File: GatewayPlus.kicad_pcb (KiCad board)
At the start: 2 copper layers, 104.7 x 63.4 mm, 31 parts, among them J1 LTDC_LCD_FPC_40p, SW1 SW_Push, U1 STM32F429IGTx, U2 IS42S16400J - HY57V641620E, U3 W25Q128JVS, Y1 32.768KHz, Y2 25MHz

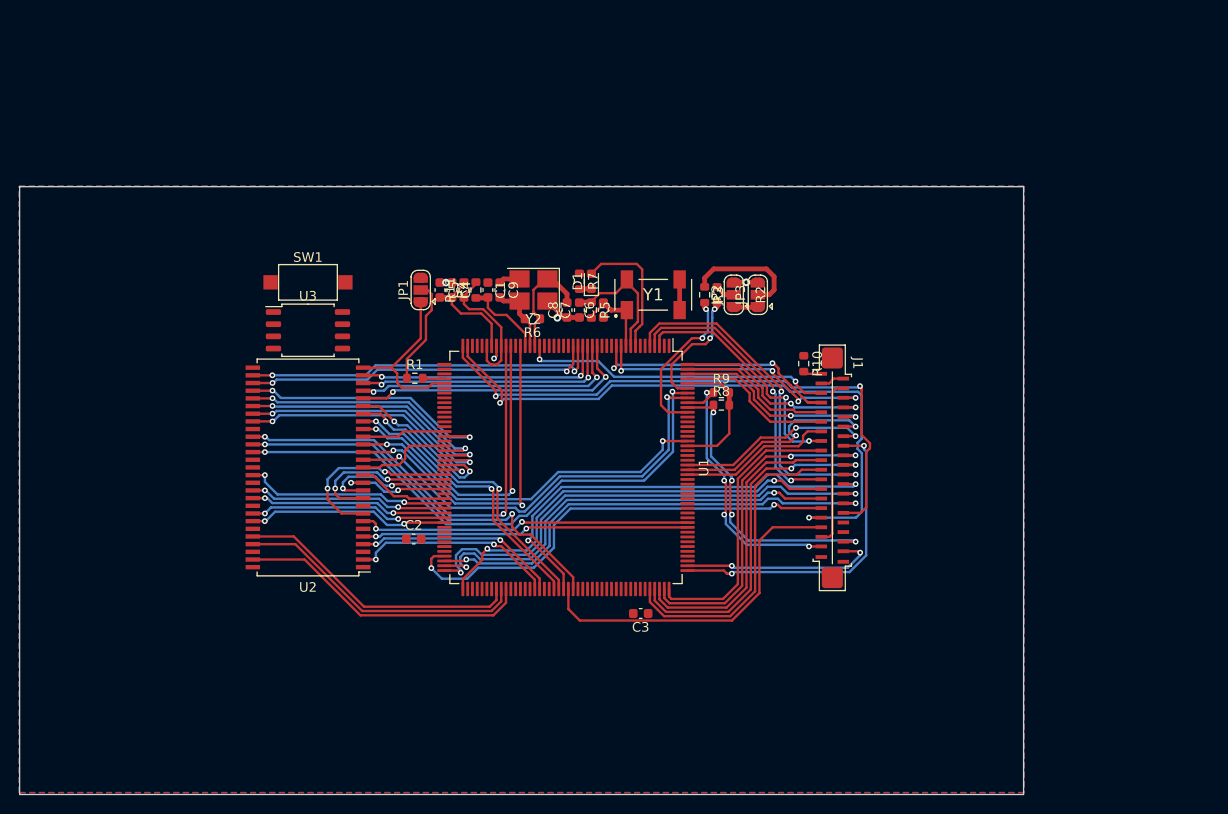
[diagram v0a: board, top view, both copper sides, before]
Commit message: Add WiFi block and finished WiFi layout
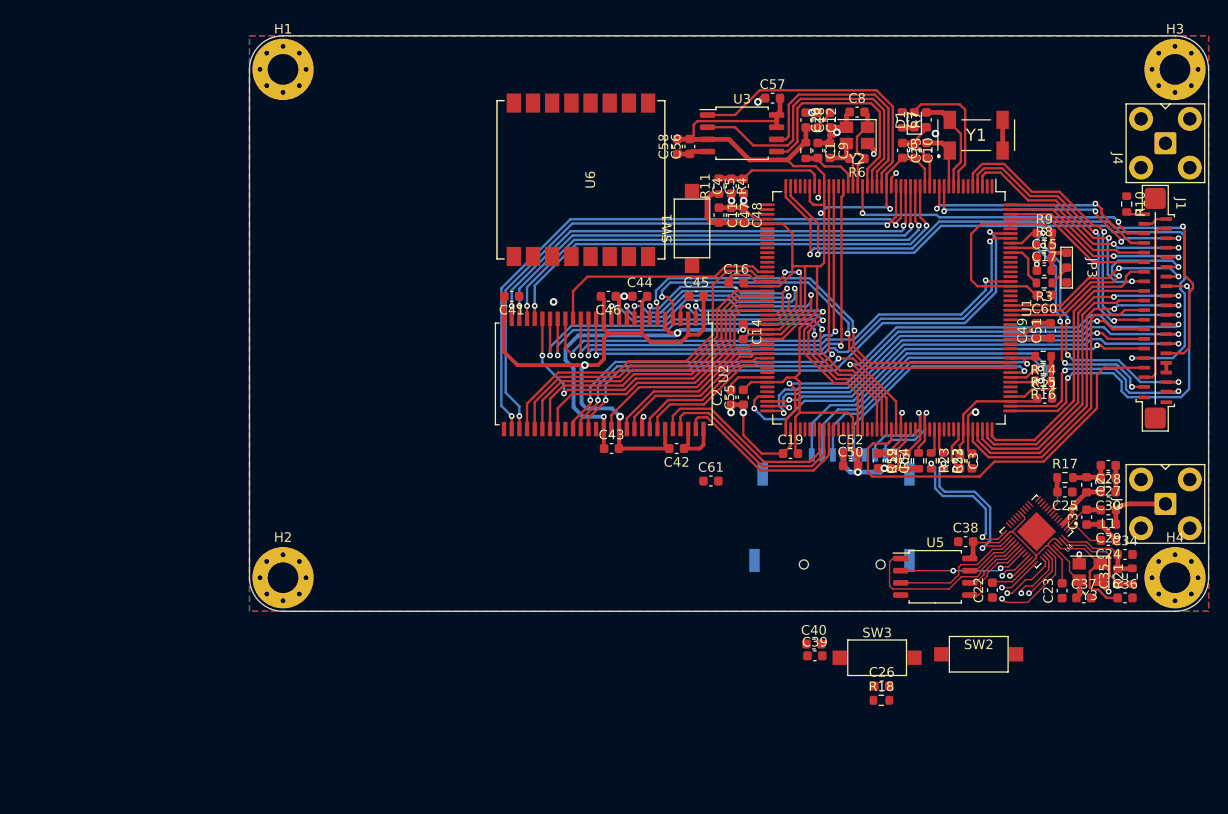
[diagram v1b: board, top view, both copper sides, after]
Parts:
- removed JP1: BYPASS, Jumper:SolderJumper-3_P1.3mm_Open_RoundedPad1.0x1.5mm
- removed JP2: PDR, Jumper:SolderJumper-3_P1.3mm_Open_RoundedPad1.0x1.5mm
- removed R1, R2: R_Small, Resistor_SMD:R_0603_1608Metric
- added C10: 1uF, Capacitor_SMD:C_0603_1608Metric, F.Cu at (169.3, 62.0)
- added C11: 100nF, Capacitor_SMD:C_0603_1608Metric, F.Cu at (148.9, 68.7)
- added C12: 100nF, Capacitor_SMD:C_0603_1608Metric, F.Cu at (159.3, 58.8)
- added C13: 100nF, Capacitor_SMD:C_0603_1608Metric, F.Cu at (168.1, 62.0)
- added C14: 100nF, Capacitor_SMD:C_0603_1608Metric, F.Cu at (151.5, 80.9)
- added C15: 1uF, Capacitor_SMD:C_0603_1608Metric, F.Cu at (182.9, 73.2)
- added C16: 1uF, Capacitor_SMD:C_0603_1608Metric, F.Cu at (150.7, 75.8)
- added C17: 100nF, Capacitor_SMD:C_0603_1608Metric, F.Cu at (182.9, 74.5)
- added C18: 1uF, Capacitor_SMD:C_0603_1608Metric, F.Cu at (158.0, 58.8)
- added C19: 100nF, Capacitor_SMD:C_0603_1608Metric, F.Cu at (156.4, 93.5)
- added C20: 100nF, Capacitor_SMD:C_0603_1608Metric, F.Cu at (160.5, 58.8)
- added C21: 100nF, Capacitor_SMD:C_0603_1608Metric, F.Cu at (182.9, 87.8)
- added C22: 1uF, Capacitor_SMD:C_0603_1608Metric, F.Cu at (177.5, 107.8)
- added C23: 100nF, Capacitor_SMD:C_0603_1608Metric, F.Cu at (184.7, 107.8)
- added C24: 100nF, Capacitor_SMD:C_0603_1608Metric, F.Cu at (189.6, 102.6)
- added C25: C_Small, Capacitor_SMD:C_0603_1608Metric, F.Cu at (185.0, 97.6)
- added C26: C_Small, Capacitor_SMD:C_0603_1608Metric, F.Cu at (165.9, 117.8)
- added C27: 1uF, Capacitor_SMD:C_0603_1608Metric, F.Cu at (189.5, 96.0)
- added C28: 100nF, Capacitor_SMD:C_0603_1608Metric, F.Cu at (189.5, 94.8)
- added C29: 100nF, Capacitor_SMD:C_0603_1608Metric, F.Cu at (189.6, 100.9)
- added C30: 100nF, Capacitor_SMD:C_0603_1608Metric, F.Cu at (189.5, 97.6)
- added C31: 100nF, Capacitor_SMD:C_0603_1608Metric, F.Cu at (187.3, 100.2)
- added C34: 100nF, Capacitor_SMD:C_0603_1608Metric, F.Cu at (191.3, 104.1)
- added C35: 100nF, Capacitor_SMD:C_0603_1608Metric, F.Cu at (190.5, 106.3)
- added C36: 100nF, Capacitor_SMD:C_0603_1608Metric, F.Cu at (191.3, 108.6)
- added C37: 100nF, Capacitor_SMD:C_0603_1608Metric, F.Cu at (187.0, 108.6)
- added C38: 1uF, Capacitor_SMD:C_0603_1608Metric, F.Cu at (174.7, 102.7)
- added C39: 100nF, Capacitor_SMD:C_0603_1608Metric, F.Cu at (158.9, 114.6)
- added C40: 100nF, Capacitor_SMD:C_0603_1608Metric, F.Cu at (158.8, 113.4)
- added C41: 1uF, Capacitor_SMD:C_0603_1608Metric, F.Cu at (127.3, 77.2)
- added C42: 100nF, Capacitor_SMD:C_0603_1608Metric, F.Cu at (144.5, 93.0)
- added C43: 100nF, Capacitor_SMD:C_0603_1608Metric, F.Cu at (137.8, 93.0)
- added C44: 1uF, Capacitor_SMD:C_0603_1608Metric, F.Cu at (140.7, 77.2)
- added C45: 100nF, Capacitor_SMD:C_0603_1608Metric, F.Cu at (146.6, 77.1)
- added C46: 100nF, Capacitor_SMD:C_0603_1608Metric, F.Cu at (137.4, 77.2)
- added C47: 1uF, Capacitor_SMD:C_0603_1608Metric, F.Cu at (150.2, 68.7)
- added C48: 100nF, Capacitor_SMD:C_0603_1608Metric, F.Cu at (151.5, 68.7)
- added C49: 100nF, Capacitor_SMD:C_0603_1608Metric, F.Cu at (182.0, 80.7)
- added C50: 1uF, Capacitor_SMD:C_0603_1608Metric, F.Cu at (162.7, 94.8)
- added C51: 100nF, Capacitor_SMD:C_0603_1608Metric, F.Cu at (183.5, 80.7)
- added C52: 100nF, Capacitor_SMD:C_0603_1608Metric, F.Cu at (162.7, 93.5)
- added C53: 1uF, Capacitor_SMD:C_0603_1608Metric, F.Cu at (175.3, 94.3)
- added C54: 100nF, Capacitor_SMD:C_0603_1608Metric, F.Cu at (166.8, 94.3)
- added C55: 100nF, Capacitor_SMD:C_0603_1608Metric, F.Cu at (151.5, 87.7)
- added C56: 1uF, Capacitor_SMD:C_0603_1608Metric, F.Cu at (145.9, 61.5)
- added C57: 100nF, Capacitor_SMD:C_0603_1608Metric, F.Cu at (154.5, 56.5)
- added C58: 100nF, Capacitor_SMD:C_0603_1608Metric, F.Cu at (144.6, 61.5)
- added C59: 1uF, Capacitor_SMD:C_0603_1608Metric, F.Cu at (165.6, 94.3)
- added C60: 100nF, Capacitor_SMD:C_0603_1608Metric, F.Cu at (182.9, 77.0)
- added C61: 100nF, Capacitor_SMD:C_0603_1608Metric, F.Cu at (148.1, 96.4)
- added H1: Hole, MountingHole:MountingHole_3.2mm_M3_Pad_Via, F.Cu at (103.5, 53.5)
- added H2: Hole, MountingHole:MountingHole_3.2mm_M3_Pad_Via, F.Cu at (103.5, 106.5)
- added H3: Hole, MountingHole:MountingHole_3.2mm_M3_Pad_Via, F.Cu at (196.5, 53.5)
- added H4: Hole, MountingHole:MountingHole_3.2mm_M3_Pad_Via, F.Cu at (196.5, 106.5)
- added J2: Micro_SD_Card, Anh_Footprints:MicroSD_Socket, B.Cu at (161.2, 105.1)
- added J3: ESP Anten, Anh_Footprints:Connector_Coaxial_SMA, F.Cu at (195.5, 98.8)
- added J4: xAnt, Anh_Footprints:Connector_Coaxial_SMA, F.Cu at (195.5, 61.2)
- added L1: L_Small, Inductor_SMD:L_0603_1608Metric, F.Cu at (189.6, 99.4)
- added L2: L_Small, Inductor_SMD:L_0603_1608Metric, F.Cu at (187.3, 96.8)
- added R12: R_Small, Resistor_SMD:R_0603_1608Metric, F.Cu at (168.5, 94.3)
- added R14: R_Small, Resistor_SMD:R_0603_1608Metric, F.Cu at (182.8, 83.4)
- added R15: R_Small, Resistor_SMD:R_0603_1608Metric, F.Cu at (182.8, 84.7)
- added R16: R_Small, Resistor_SMD:R_0603_1608Metric, F.Cu at (182.8, 86.0)
- added R17: R_Small, Resistor_SMD:R_0603_1608Metric, F.Cu at (185.0, 96.1)
- added R18: R_Small, Resistor_SMD:R_0603_1608Metric, F.Cu at (165.9, 119.3)
- added R21: R_Small, Resistor_SMD:R_0603_1608Metric, F.Cu at (192.0, 106.3)
- added R22: R_Small, Resistor_SMD:R_0603_1608Metric, F.Cu at (172.4, 94.3)
- added R23: R_Small, Resistor_SMD:R_0603_1608Metric, F.Cu at (171.1, 94.3)
- added SW2: ESP_RESET, Button_Switch_SMD:SW_SPST_CK_RS282G05A3, F.Cu at (176.0, 114.5)
- added SW3: ESP_BOOT, Button_Switch_SMD:SW_SPST_CK_RS282G05A3, F.Cu at (165.4, 114.8)
- added U4: ESP32-D0WD-V3, Anh_Footprints:ESP32-QFN48, F.Cu at (182.1, 101.7)
- added U5: W25Q32JVSS, Package_SO:SOIC-8_5.23x5.23mm_P1.27mm, F.Cu at (171.5, 106.4)
- added U6: Ai-Thinker-Ra-02, RF_Module:Ai-Thinker-Ra-01-LoRa, F.Cu at (134.6, 65.0)
- added Y3: 40MHz, Crystal:Crystal_SMD_3225-4Pin_3.2x2.5mm, F.Cu at (187.6, 105.9)
- C6, C7: value C_Small -> 22pF
- JP3: value PDR -> BOOT; footprint Jumper:SolderJumper-3_P1.3mm_Open_RoundedPad1.0x1.5mm -> Anh_Footprints:Jump3_0603_Open
- Y2: footprint Crystal:Crystal_SMD_3225-4Pin_3.2x2.5mm_HandSoldering -> Crystal:Crystal_SMD_3225-4Pin_3.2x2.5mm
- moved U3 49.7 mm to (151.4, 60.2)
- moved C7 41.2 mm to (170.6, 58.8)
- moved SW1 40.4 mm to (146.1, 70.1), turned to 90 degrees
- moved R6 37.7 mm to (163.3, 62.8)
- moved D1 37.6 mm to (169.3, 58.8)
- moved R7 37.6 mm to (168.1, 58.8)
- moved R5 37.6 mm to (169.8, 94.3), turned to 90 degrees
- moved R10 37.6 mm to (191.5, 67.5)
- moved R8 37.6 mm to (182.9, 71.9)
- moved R9 37.6 mm to (182.9, 70.6)
- moved Y1 37.6 mm to (175.8, 60.4)
- moved C6 37.6 mm to (170.6, 62.0)
- moved J1 37.6 mm to (193.3, 68.6)
- moved U1 37.6 mm to (166.7, 78.4)
- moved Y2 37.4 mm to (163.3, 60.4)
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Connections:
- net /FLASH_SDRAM/SDRAM_A0 renamed /MCU/SDRAM_A0
- net /FLASH_SDRAM/SDRAM_A1 renamed /MCU/SDRAM_A1
- net /FLASH_SDRAM/SDRAM_A10 renamed /MCU/SDRAM_A10
- net /FLASH_SDRAM/SDRAM_A11 renamed /MCU/SDRAM_A11
- net /FLASH_SDRAM/SDRAM_A2 renamed /MCU/SDRAM_A2
- net /FLASH_SDRAM/SDRAM_A3 renamed /MCU/SDRAM_A3
- net /FLASH_SDRAM/SDRAM_A4 renamed /MCU/SDRAM_A4
- net /FLASH_SDRAM/SDRAM_A5 renamed /MCU/SDRAM_A5
- net /FLASH_SDRAM/SDRAM_A6 renamed /MCU/SDRAM_A6
- net /FLASH_SDRAM/SDRAM_A7 renamed /MCU/SDRAM_A7
- net /FLASH_SDRAM/SDRAM_A8 renamed /MCU/SDRAM_A8
- net /FLASH_SDRAM/SDRAM_A9 renamed /MCU/SDRAM_A9
- net /FLASH_SDRAM/SDRAM_BA0 renamed /MCU/SDRAM_BA0
- net /FLASH_SDRAM/SDRAM_BA1 renamed /MCU/SDRAM_BA1
- net /FLASH_SDRAM/SDRAM_CKE renamed /MCU/SDRAM_CKE
- net /FLASH_SDRAM/SDRAM_CLK renamed /MCU/SDRAM_CLK
- net /FLASH_SDRAM/SDRAM_D0 renamed /MCU/SDRAM_D0
- net /FLASH_SDRAM/SDRAM_D1 renamed /MCU/SDRAM_D1
- net /FLASH_SDRAM/SDRAM_D10 renamed /MCU/SDRAM_D10
- net /FLASH_SDRAM/SDRAM_D11 renamed /MCU/SDRAM_D11
- net /FLASH_SDRAM/SDRAM_D12 renamed /MCU/SDRAM_D12
- net /FLASH_SDRAM/SDRAM_D13 renamed /MCU/SDRAM_D13
- net /FLASH_SDRAM/SDRAM_D14 renamed /MCU/SDRAM_D14
- net /FLASH_SDRAM/SDRAM_D15 renamed /MCU/SDRAM_D15
- net /FLASH_SDRAM/SDRAM_D2 renamed /MCU/SDRAM_D2
- net /FLASH_SDRAM/SDRAM_D3 renamed /MCU/SDRAM_D3
- net /FLASH_SDRAM/SDRAM_D4 renamed /MCU/SDRAM_D4
- net /FLASH_SDRAM/SDRAM_D5 renamed /MCU/SDRAM_D5
- net /FLASH_SDRAM/SDRAM_D6 renamed /MCU/SDRAM_D6
- net /FLASH_SDRAM/SDRAM_D7 renamed /MCU/SDRAM_D7
- net /FLASH_SDRAM/SDRAM_D8 renamed /MCU/SDRAM_D8
- net /FLASH_SDRAM/SDRAM_D9 renamed /MCU/SDRAM_D9
- net /FLASH_SDRAM/SDRAM_NBL0 renamed /MCU/SDRAM_NBL0
- net /FLASH_SDRAM/SDRAM_NBL1 renamed /MCU/SDRAM_NBL1
- net /FLASH_SDRAM/SDRAM_NCAS renamed /MCU/SDRAM_NCAS
- net /FLASH_SDRAM/SDRAM_NE renamed /MCU/SDRAM_NE
- net /FLASH_SDRAM/SDRAM_NRAS renamed /MCU/SDRAM_NRAS
- net /FLASH_SDRAM/SDRAM_NWE renamed /MCU/SDRAM_NWE
- net /LTDC_LCD/LTDC_B0 renamed /LTDC TFT LCD/LTDC_B0
- net /LTDC_LCD/LTDC_B1 renamed /LTDC TFT LCD/LTDC_B1
- net /LTDC_LCD/LTDC_B2 renamed /LTDC TFT LCD/LTDC_B2
- net /LTDC_LCD/LTDC_B3 renamed /LTDC TFT LCD/LTDC_B3
- net /LTDC_LCD/LTDC_B4 renamed /LTDC TFT LCD/LTDC_B4
- net /LTDC_LCD/LTDC_B5 renamed /LTDC TFT LCD/LTDC_B5
- net /LTDC_LCD/LTDC_B6 renamed /LTDC TFT LCD/LTDC_B6
- net /LTDC_LCD/LTDC_B7 renamed /LTDC TFT LCD/LTDC_B7
- net /LTDC_LCD/LTDC_DE renamed /LTDC TFT LCD/LTDC_DE
- net /LTDC_LCD/LTDC_G0 renamed /LTDC TFT LCD/LTDC_G0
- net /LTDC_LCD/LTDC_G1 renamed /LTDC TFT LCD/LTDC_G1
- net /LTDC_LCD/LTDC_G2 renamed /LTDC TFT LCD/LTDC_G2
- net /LTDC_LCD/LTDC_G3 renamed /LTDC TFT LCD/LTDC_G3
- net /LTDC_LCD/LTDC_G4 renamed /LTDC TFT LCD/LTDC_G4
- net /LTDC_LCD/LTDC_G5 renamed /LTDC TFT LCD/LTDC_G5
- net /LTDC_LCD/LTDC_G6 renamed /LTDC TFT LCD/LTDC_G6
- net /LTDC_LCD/LTDC_G7 renamed /LTDC TFT LCD/LTDC_G7
- net /LTDC_LCD/LTDC_HSYNC renamed /LTDC TFT LCD/LTDC_HSYNC
- net /LTDC_LCD/LTDC_PCLK renamed /LTDC TFT LCD/LTDC_PCLK
- net /LTDC_LCD/LTDC_R0 renamed /LTDC TFT LCD/LTDC_R0
- net /LTDC_LCD/LTDC_R1 renamed /LTDC TFT LCD/LTDC_R1
- net /LTDC_LCD/LTDC_R2 renamed /LTDC TFT LCD/LTDC_R2
- net /LTDC_LCD/LTDC_R3 renamed /LTDC TFT LCD/LTDC_R3
- net /LTDC_LCD/LTDC_R4 renamed /LTDC TFT LCD/LTDC_R4
- net /LTDC_LCD/LTDC_R5 renamed /LTDC TFT LCD/LTDC_R5
- net /LTDC_LCD/LTDC_R6 renamed /LTDC TFT LCD/LTDC_R6
- net /LTDC_LCD/LTDC_R7 renamed /LTDC TFT LCD/LTDC_R7
- net /LTDC_LCD/LTDC_VSYNC renamed /LTDC TFT LCD/LTDC_VSYNC
- net /LTDC_LCD/TOUCH_INT renamed /LTDC TFT LCD/TOUCH_INT
- net /LTDC_LCD/TOUCH_SCL renamed /LTDC TFT LCD/TOUCH_SCL
- net /LTDC_LCD/TOUCH_SDA renamed /LTDC TFT LCD/TOUCH_SDA
- J1 pad 35: +3V3 -> +3.3V
- J1 pad 4: +3V3 -> +3.3V
- R10 pad 1: /LTDC_LCD/LCD_BACKGROUND_LED -> /LTDC TFT LCD/LCD_BACKGROUND_LED
- R5 pad 1: LSEI -> +3.3V
- R5 pad 2: LSEO -> /MCU/SDIO_D1
- U1 pad 101: /LTDC_LCD/LCD_BACKGROUND_LED -> unconnected-(U1-Pad101)
- U1 pad 117: unconnected-(U1-Pad117) -> /MCU/SDIO_D0
- U1 pad 118: unconnected-(U1-Pad118) -> /MCU/SDIO_D1
- U1 pad 120: /MCU/USB_OTG_VBUS -> /MCU/USART1_TX
- U1 pad 121: unconnected-(U1-Pad121) -> /MCU/USART1_RX
- U1 pad 138: unconnected-(U1-Pad138) -> /LTDC TFT LCD/LCD_BACKGROUND_LED
- U1 pad 139: unconnected-(U1-Pad139) -> /MCU/SDIO_D2
- U1 pad 140: unconnected-(U1-Pad140) -> /MCU/SDIO_D3
- U1 pad 141: unconnected-(U1-Pad141) -> /MCU/SDIO_CLK
- U1 pad 144: unconnected-(U1-Pad144) -> /MCU/SDIO_CMD
- U1 pad 171: Net-(R2-Pad2) -> +3.3V
- U1 pad 24: unconnected-(U1-Pad24) -> /MCU/FLASH_CS
- U1 pad 25: unconnected-(U1-Pad25) -> /MCU/SPI1_SCK
- U1 pad 26: unconnected-(U1-Pad26) -> /MCU/SPI1_MISO
- U1 pad 27: unconnected-(U1-Pad27) -> /MCU/SPI1_MOSI
- U1 pad 48: Net-(R1-Pad2) -> GND
- U3 pad 1: /FLASH_SDRAM/SPIFLS_CS -> /MCU/FLASH_CS
- U3 pad 2: /FLASH_SDRAM/SPIFLS_DO -> /MCU/SPI1_MISO
- U3 pad 5: /FLASH_SDRAM/SPIFLS_DI -> /MCU/SPI1_MOSI
- U3 pad 6: /FLASH_SDRAM/SPIFLS_CLK -> /MCU/SPI1_SCK
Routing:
- net +3.3V: track 59.1 -> 326.1 mm, vias 0 -> 7
- net GND: track 29.7 -> 160.3 mm, vias 6 -> 23
- net /MCU/SDIO_D2: track 0.00 -> 36.3 mm, vias 0 -> 1
- net /MCU/SDIO_D3: track 0.00 -> 32.9 mm, vias 0 -> 1
- net /MCU/SPI1_MISO: track 0.00 -> 32.2 mm
- net /MCU/FLASH_CS: track 0.00 -> 29.9 mm
- net /MCU/SDIO_CMD: track 0.00 -> 29.5 mm, vias 0 -> 1
- net /MCU/SDRAM_A4: track 37.1 -> 63.9 mm
- net /MCU/SDRAM_A5: track 36.3 -> 62.3 mm
- net /MCU/SDIO_CLK: track 0.00 -> 25.2 mm, vias 0 -> 1
- net /MCU/SDRAM_A3: track 26.0 -> 51.1 mm
- net /MCU/SPI1_SCK: track 0.00 -> 24.8 mm
- net /MCU/SDRAM_A2: track 27.3 -> 51.1 mm
- net /MCU/SPI1_MOSI: track 0.00 -> 23.6 mm
- net /MCU/SDRAM_D7: track 9.49 -> 32.3 mm, vias 0 -> 2
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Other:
- board size 104.7 x 63.4 mm -> 100 x 60 mm

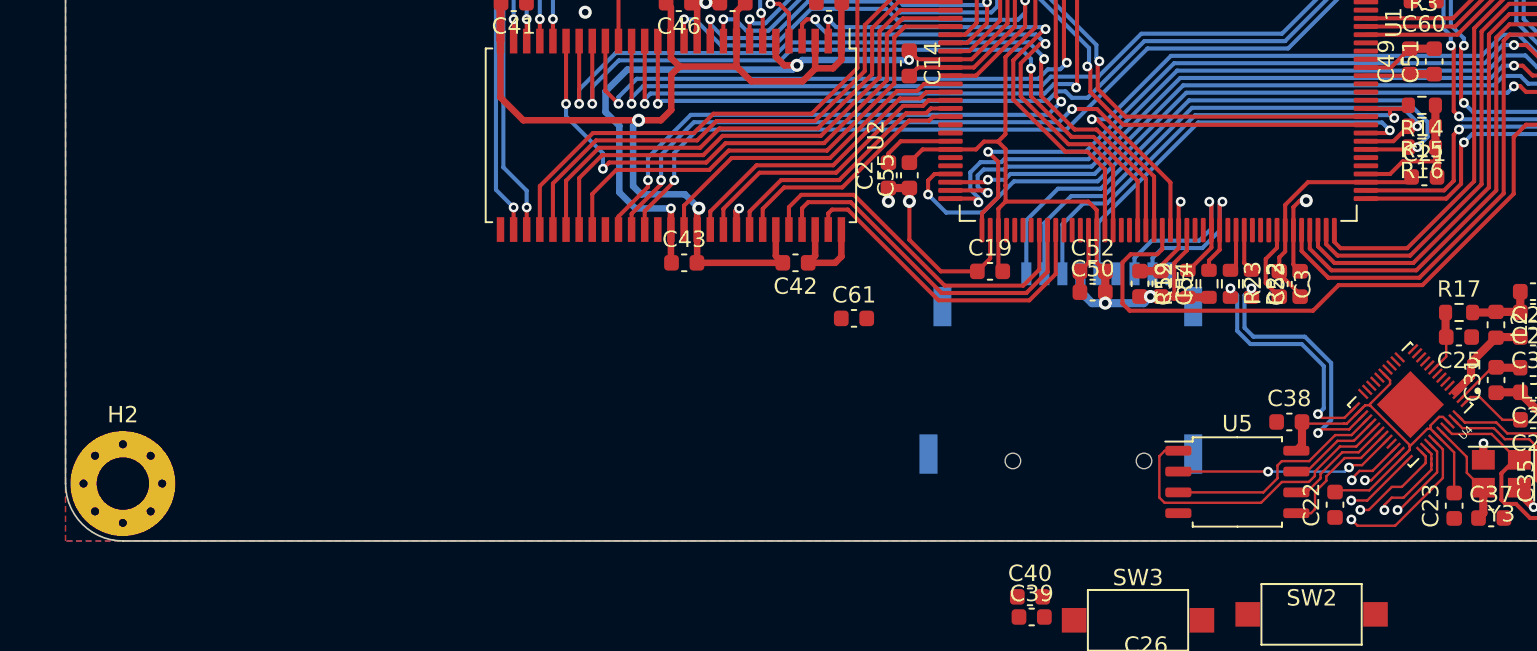
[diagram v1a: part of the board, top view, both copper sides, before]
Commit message: Add Ethernet LAN8720 Layout.
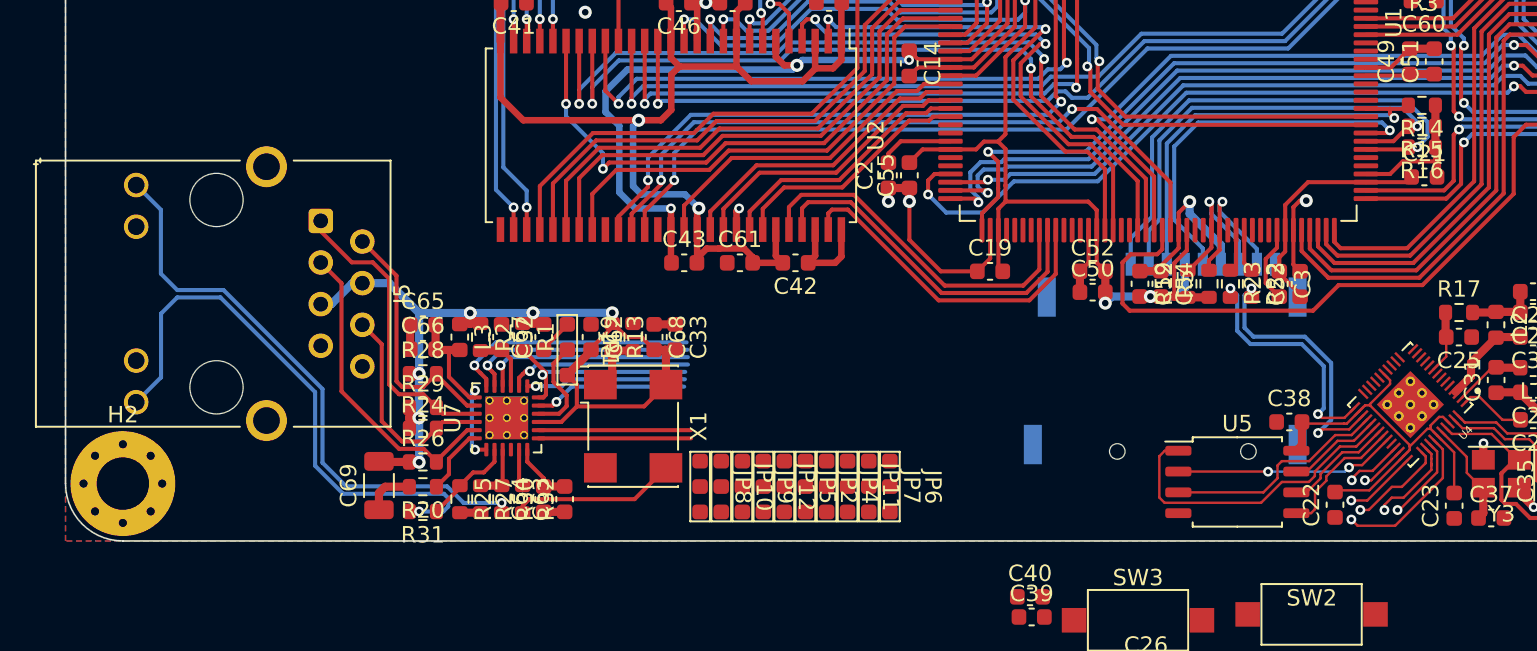
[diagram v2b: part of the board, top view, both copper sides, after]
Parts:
- added C32: C_Small, Capacitor_SMD:C_0603_1608Metric, F.Cu at (126.6, 97.6)
- added C33: C_Small, Capacitor_SMD:C_0603_1608Metric, F.Cu at (137.2, 97.6)
- added C62: C_Small, Capacitor_SMD:C_0603_1608Metric, F.Cu at (132.1, 97.6)
- added C63: C_Small, Capacitor_SMD:C_0603_1608Metric, F.Cu at (130.5, 107.5)
- added C64: C_Small, Capacitor_SMD:C_0603_1608Metric, F.Cu at (129.2, 107.5)
- added C65: C_Small, Capacitor_SMD:C_0603_1608Metric, F.Cu at (121.8, 96.8)
- added C66: C_Small, Capacitor_SMD:C_0603_1608Metric, F.Cu at (121.8, 98.3)
- added C67: C_Small, Capacitor_SMD:C_0603_1608Metric, F.Cu at (129.2, 97.6)
- added C68: C_Small, Capacitor_SMD:C_0603_1608Metric, F.Cu at (135.9, 97.6)
- added C69: C_Small, Capacitor_SMD:C_1206_3216Metric, F.Cu at (119.1, 106.6)
- added J5: HR911105A, Connector_RJ:RJ45_Hanrun_HR911105A, F.Cu at (115.6, 90.5)
- added JP1: PHYADDR, Anh_Footprints:Jump3_0603_Open, F.Cu at (130.6, 98.4)
- added JP10: J_MDC, Anh_Footprints:Jump3_0603_Open, F.Cu at (140.0, 106.7)
- added JP11: J_CLKEN, Anh_Footprints:Jump3_0603_Open, F.Cu at (147.7, 106.7)
- added JP12: J_REFCLK, Anh_Footprints:Jump3_0603_Open, F.Cu at (142.6, 106.7)
- added JP2: J_TXD0, Anh_Footprints:Jump3_0603_Open, F.Cu at (145.2, 106.7)
- added JP4: J_TXD1, Anh_Footprints:Jump3_0603_Open, F.Cu at (146.4, 106.7)
- added JP5: J_TXEN, Anh_Footprints:Jump3_0603_Open, F.Cu at (143.9, 106.7)
- added JP6: J_RXD0, Anh_Footprints:Jump3_0603_Open, F.Cu at (150.3, 106.7)
- added JP7: J_RXD1, Anh_Footprints:Jump3_0603_Open, F.Cu at (149.0, 106.7)
- added JP8: J_CRS_DV, Anh_Footprints:Jump3_0603_Open, F.Cu at (138.7, 106.7)
- added JP9: J_MDIO, Anh_Footprints:Jump3_0603_Open, F.Cu at (141.3, 106.7)
- added L3: L_Small, Inductor_SMD:L_0603_1608Metric, F.Cu at (124.1, 97.6)
- added R1: R_Small, Resistor_SMD:R_0603_1608Metric, F.Cu at (127.9, 97.6)
- added R13: R_Small, Resistor_SMD:R_0603_1608Metric, F.Cu at (133.4, 97.6)
- added R19: R_Small, Resistor_SMD:R_0603_1608Metric, F.Cu at (134.6, 97.6)
- added R2: R_Small, Resistor_SMD:R_0603_1608Metric, F.Cu at (125.3, 97.6)
- added R20: R_Small, Resistor_SMD:R_0603_1608Metric, F.Cu at (121.8, 106.7)
- added R24: R_Small, Resistor_SMD:R_0603_1608Metric, F.Cu at (121.8, 103.1)
- added R25: R_Small, Resistor_SMD:R_0603_1608Metric, F.Cu at (124.1, 107.5)
- added R26: R_Small, Resistor_SMD:R_0603_1608Metric, F.Cu at (121.8, 105.2)
- added R27: R_Small, Resistor_SMD:R_0603_1608Metric, F.Cu at (125.3, 107.5)
- added R28: R_Small, Resistor_SMD:R_0603_1608Metric, F.Cu at (121.8, 99.8)
- added R29: R_Small, Resistor_SMD:R_0603_1608Metric, F.Cu at (121.8, 101.8)
- added R30: R_Small, Resistor_SMD:R_0603_1608Metric, F.Cu at (126.6, 107.5)
- added R31: R_Small, Resistor_SMD:R_0603_1608Metric, F.Cu at (121.8, 108.2)
- added R32: R_Small, Resistor_SMD:R_0603_1608Metric, F.Cu at (127.9, 107.5)
- added U7: LAN8720A, Package_DFN_QFN:QFN-24-1EP_4x4mm_P0.5mm_EP2.6x2.6mm_ThermalVias, F.Cu at (126.9, 102.5)
- added X1: 50MHz, Oscillator:Oscillator_SMD_Abracon_ASV-4Pin_7.0x5.1mm, F.Cu at (134.6, 103.0)
- moved C61 7.74 mm to (141.2, 93.0)
- moved J2 6.40 mm to (167.6, 104.5)
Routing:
- net +3V3: track 0.00 -> 60.3 mm, vias 0 -> 6
- net Net-(J5-Pad9): track 0.00 -> 35.8 mm, vias 0 -> 1
- net Net-(J5-Pad12): track 0.00 -> 34.7 mm, vias 0 -> 1
- net Net-(J5-Pad3): track 0.00 -> 19.2 mm
- net Net-(J5-Pad1): track 0.00 -> 19.0 mm
- net Net-(J5-Pad2): track 0.00 -> 15.5 mm
- net GND: track 160.3 -> 175.7 mm
- net /ETH/RMII_TXD1: track 0.00 -> 15.1 mm, vias 0 -> 1
- net /ETH/RMII_TXD0: track 0.00 -> 14.1 mm, vias 0 -> 1
- net Net-(J5-Pad6): track 0.00 -> 13.1 mm
- net /ETH/RMII_TXEN: track 0.00 -> 12.9 mm, vias 0 -> 1
- net /ETH/RMII_MDIO: track 0.00 -> 12.9 mm, vias 0 -> 1
- net Net-(C65-Pad2): track 0.00 -> 11.5 mm, vias 0 -> 2
- net /ETH/ETH_REFCLK: track 0.00 -> 11.1 mm, vias 0 -> 1
- net Net-(R32-Pad2): track 0.00 -> 10.1 mm
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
